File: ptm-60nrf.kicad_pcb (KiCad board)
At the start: 2 copper layers, 285 x 94.6 mm, 160 parts, among them J1 USB_C_Receptacle_USB2.0, J2 BAT, J4 SWD, Q1 AO3407, U1 TP4054, U2 XC6220B331MR-G, U3 nRF52840_holyiot_18010, U4 SRV05-4, Y1 32.768Hz

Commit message: fixed schematic flaws and caps lock (thanks Martin!)
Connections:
- MX32 pad 1: COL0 -> Net-(D33-Pad2)
- MX32 pad 2: Net-(D33-Pad2) -> COL0
- MX61 pad 1: Net-(MX61-Pad1) -> COL12
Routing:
- net COL0: track 282.5 -> 291.7 mm
- net Net-(D33-Pad2): track 15.7 -> 17.0 mm

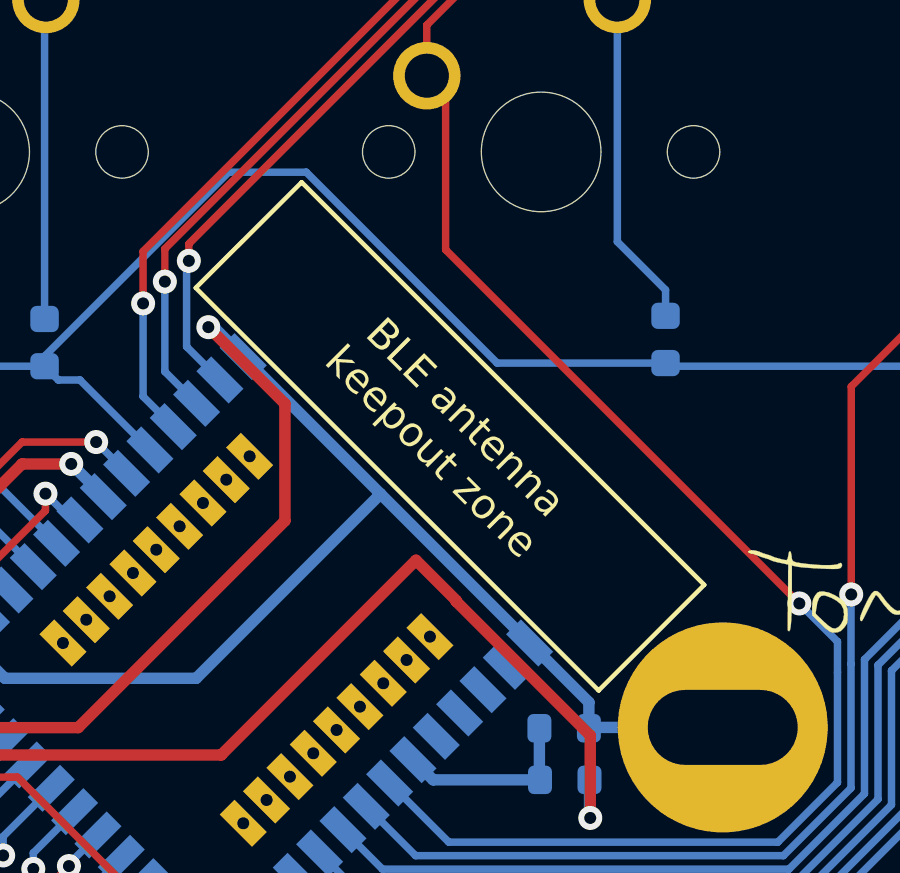
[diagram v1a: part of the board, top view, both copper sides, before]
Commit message: added hole for antenna
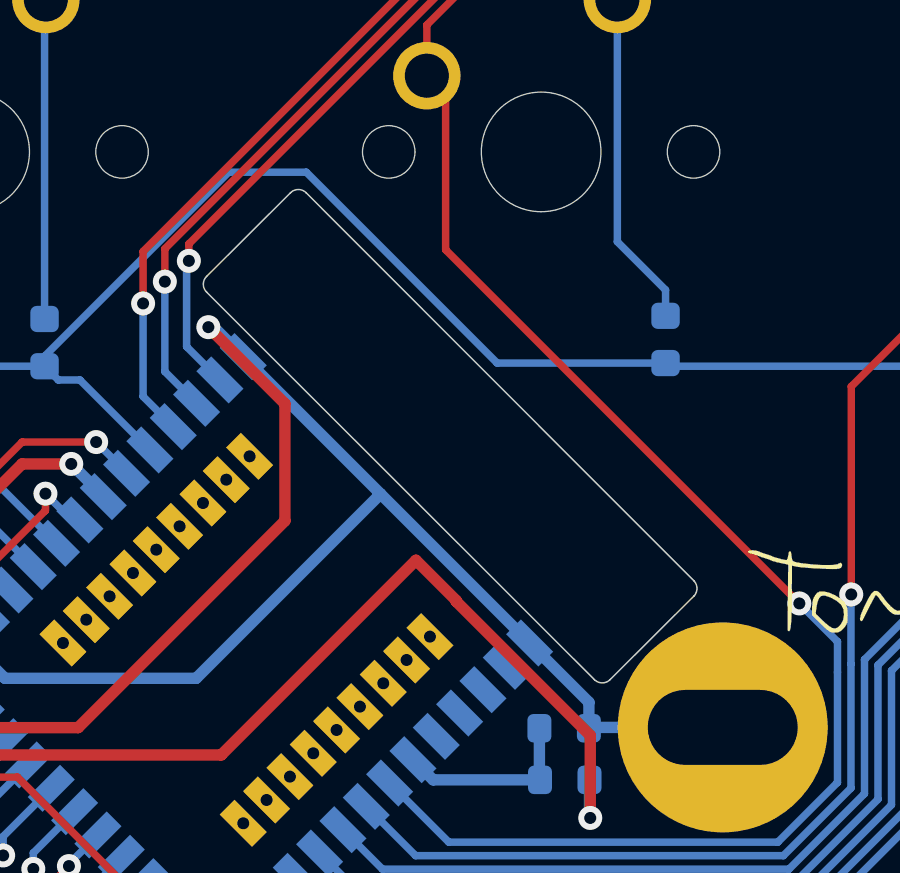
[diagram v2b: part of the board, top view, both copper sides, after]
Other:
- outline, holes or cut-outs redrawn
- board text removed: "BLE antenna keepout zone"
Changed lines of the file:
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@@
   (general
     (thickness 1.6)
-    (drawings 40)
+    (drawings 38)
     (tracks 951)
     (zones 0)
@@
     )
   )
+  (gr_line (start 209.599999 99.259999) (end 206.809999 102.039999) (layer Edge.Cuts) (width 0.05))
+  (gr_line (start 196.679999 85.810001) (end 209.599999 98.740001) (layer Edge.Cuts) (width 0.05))
+  (gr_line (start 193.360001 88.600001) (end 196.160001 85.810001) (layer Edge.Cuts) (width 0.05))
+  (gr_line (start 206.290001 102.039999) (end 193.360001 89.119999) (layer Edge.Cuts) (width 0.05))
+  (gr_arc (start 206.55 101.78) (end 206.290001 102.039999) (angle -90) (layer Edge.Cuts) (width 0.05))
+  (gr_arc (start 209.34 99) (end 209.599999 99.259999) (angle -90) (layer Edge.Cuts) (width 0.05))
+  (gr_arc (start 196.42 86.07) (end 196.679999 85.810001) (angle -90) (layer Edge.Cuts) (width 0.05))
+  (gr_arc (start 193.62 88.86) (end 193.360001 88.600001) (angle -90) (layer Edge.Cuts) (width 0.05))
   (gr_text BTW (at 301.94 109.39 90) (layer B.Mask)
     (effects (font (size 0.35 0.35) (thickness 0.04)) (justify mirror))
@@
     (effects (font (size 0.25 0.25) (thickness 0.05) italic) (justify mirror))
   )
-  (gr_line (start 192.99 88.97) (end 206.44 102.39) (layer B.SilkS) (width 0.12))
-  (gr_line (start 196.53 85.44) (end 192.99 88.97) (layer B.SilkS) (width 0.12))
-  (gr_line (start 209.96 98.88) (end 196.53 85.44) (layer B.SilkS) (width 0.12))
-  (gr_line (start 206.44 102.39) (end 209.96 98.88) (layer B.SilkS) (width 0.12))
-  (gr_text "BLE antenna\nkeepout zone" (at 201.44 93.87 -45) (layer B.SilkS)
-    (effects (font (size 1 1) (thickness 0.15)) (justify mirror))
-  )
-  (gr_line (start 209.95 98.88) (end 196.53 85.46) (layer F.SilkS) (width 0.15))
-  (gr_line (start 206.43 102.4) (end 209.95 98.88) (layer F.SilkS) (width 0.15))
-  (gr_line (start 193 88.98) (end 206.43 102.4) (layer F.SilkS) (width 0.15))
-  (gr_line (start 196.53 85.46) (end 193 88.98) (layer F.SilkS) (width 0.15))
-  (gr_text "BLE antenna\nkeepout zone" (at 201.43 93.87 315) (layer F.SilkS)
-    (effects (font (size 1 1) (thickness 0.15)))
-  )
   (gr_text Power (at 132.89 106.23) (layer B.Mask)

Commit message: minor fixes
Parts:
- removed G***: LOGO, tomlogo:tomlogoliten
- removed the HOLE at (45.2, 46.5)
- removed the HOLE at (210.6, 103.6)
- removed the HOLE at (277.9, 46.2)
- removed the HOLE at (147.3, 65.4)
- removed the HOLE at (303.4, 74.9)
- removed the HOLE at (19.7, 75.1)
- removed Y1: 32.768Hz, Crystal:Crystal_SMD_MicroCrystal_CM9V-T1A-2Pin_1.6x1.0mm
- added HOLE: VAL**, ptm-60nrf:PKRHSL, F.Cu at (303.4, 75.0)
- added HOLE: VAL**, ptm-60nrf:PKRH, F.Cu at (277.9, 46.2)
- added HOLE: VAL**, ptm-60nrf:PKRH, F.Cu at (147.4, 65.4)
- added HOLE: VAL**, ptm-60nrf:PKRH, F.Cu at (45.2, 46.5)
- added HOLE: VAL**, ptm-60nrf:PKRHSL, F.Cu at (19.6, 75.1)
- J4: footprint Connector_PinSocket_2.54mm:PinSocket_1x03_P2.54mm_Vertical -> Connector_PinSocket_2.54mm:PinSocket_1x04_P2.54mm_Vertical
- moved D31 16.2 mm to (265.0, 37.1), turned to 270 degrees
- moved D20 15.8 mm to (59.5, 37.1), turned to 270 degrees
- moved D21 15.8 mm to (78.5, 37.1), turned to 270 degrees
- moved D22 15.8 mm to (97.6, 37.1), turned to 270 degrees
- moved D23 15.8 mm to (116.6, 37.1), turned to 270 degrees
- moved D24 15.8 mm to (135.7, 37.1), turned to 270 degrees
- moved D25 15.8 mm to (154.7, 37.1), turned to 270 degrees
- moved D26 15.8 mm to (173.8, 37.1), turned to 270 degrees
- moved D27 15.8 mm to (192.8, 37.1), turned to 270 degrees
- moved D29 15.8 mm to (230.9, 37.1), turned to 270 degrees
- moved D30 15.8 mm to (250.0, 37.1), turned to 270 degrees
- moved D28 15.8 mm to (211.9, 37.1), turned to 270 degrees
- moved D59 15.1 mm to (207.1, 75.7), turned to 270 degrees
- moved D32 14.4 mm to (280.9, 38.5), turned to 0 degrees
- moved D19 14.1 mm to (32.5, 39.1), turned to 270 degrees
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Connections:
- J4 pad 1: Net-(J4-Pad1) -> GND
- J4 pad 2: /SWDCLK -> Net-(J4-Pad2)
- J4 pad 3: GND -> /SWDCLK
- MX33 pad 1: Net-(MX33-Pad1) -> COL1
- U3 pad 26: COL7 -> Net-(U3-Pad26)
- U3 pad 28: COL8 -> COL7
- U3 pad 29: Net-(U3-Pad29) -> COL8
- U3 pad 32: Net-(J4-Pad1) -> Net-(J4-Pad2)
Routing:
- net ROW1: track 291.0 -> 318.8 mm
- net VDD: track 70.1 -> 90.9 mm, vias 2 -> 3
- net Net-(J4-Pad2): track 0.00 -> 20.0 mm, vias 0 -> 1
- net Net-(J4-Pad1): track 16.6 -> 0.00 mm, vias 1 -> 0
- net ROW3: track 274.6 -> 288.1 mm
- net COL13: track 196.4 -> 208.4 mm
- net GND: track 372.0 -> 383.3 mm, vias 19 -> 21
- net COL9: track 121.9 -> 132.8 mm
- net COL1: track 236.9 -> 245.3 mm
- net Net-(D59-Pad2): track 11.3 -> 2.93 mm
- net Net-(D28-Pad2): track 10.8 -> 3.43 mm
- net Net-(D30-Pad2): track 10.8 -> 3.43 mm
- net Net-(D29-Pad2): track 10.8 -> 3.43 mm
- net Net-(D27-Pad2): track 10.8 -> 3.43 mm
- net Net-(D26-Pad2): track 10.8 -> 3.43 mm
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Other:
- board text added: "VDD"

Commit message: restored lost artwork
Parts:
- added G***: LOGO, ptm-60nrf:tomlogoliten, F.Cu at (223.5, 104.1)

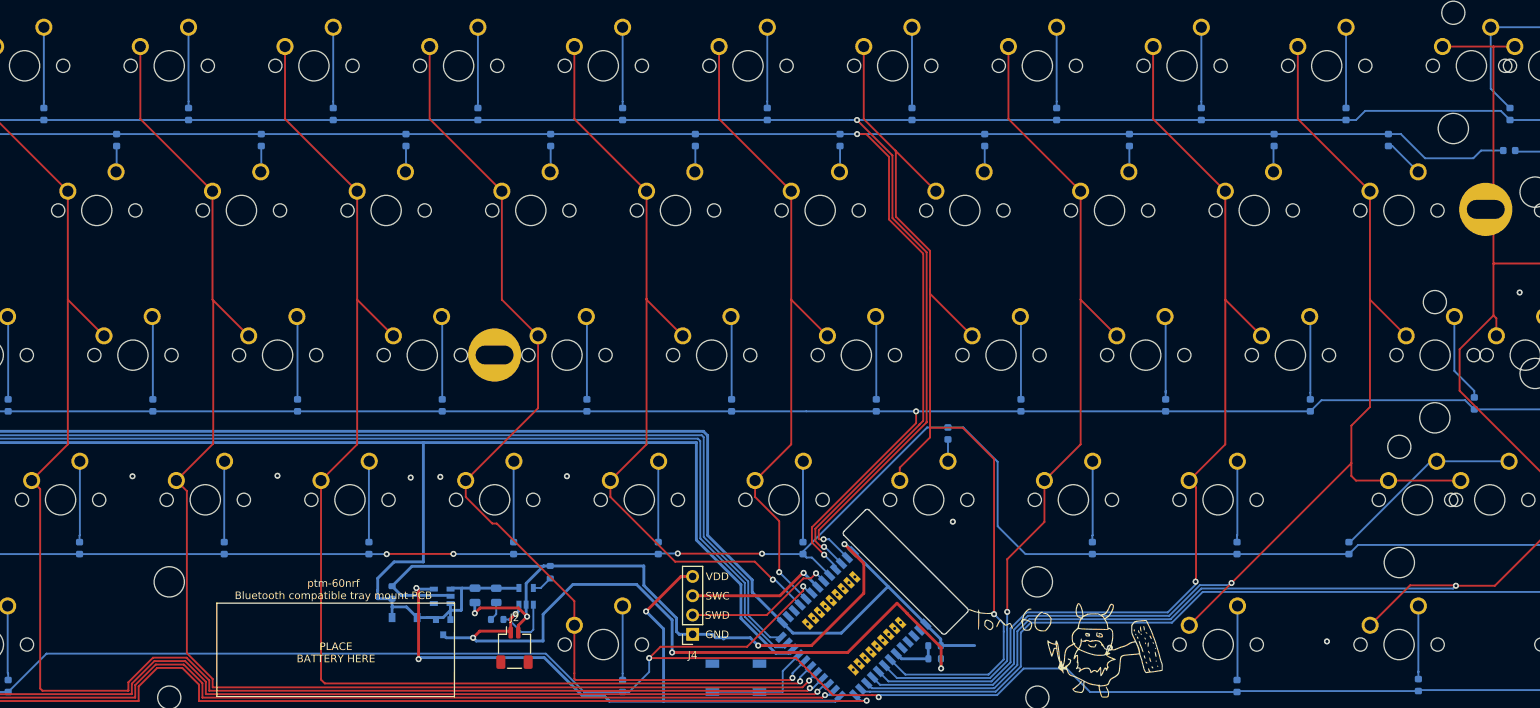
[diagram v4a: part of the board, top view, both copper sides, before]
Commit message: squashed bugs in schematic and rewired pwr/chrg
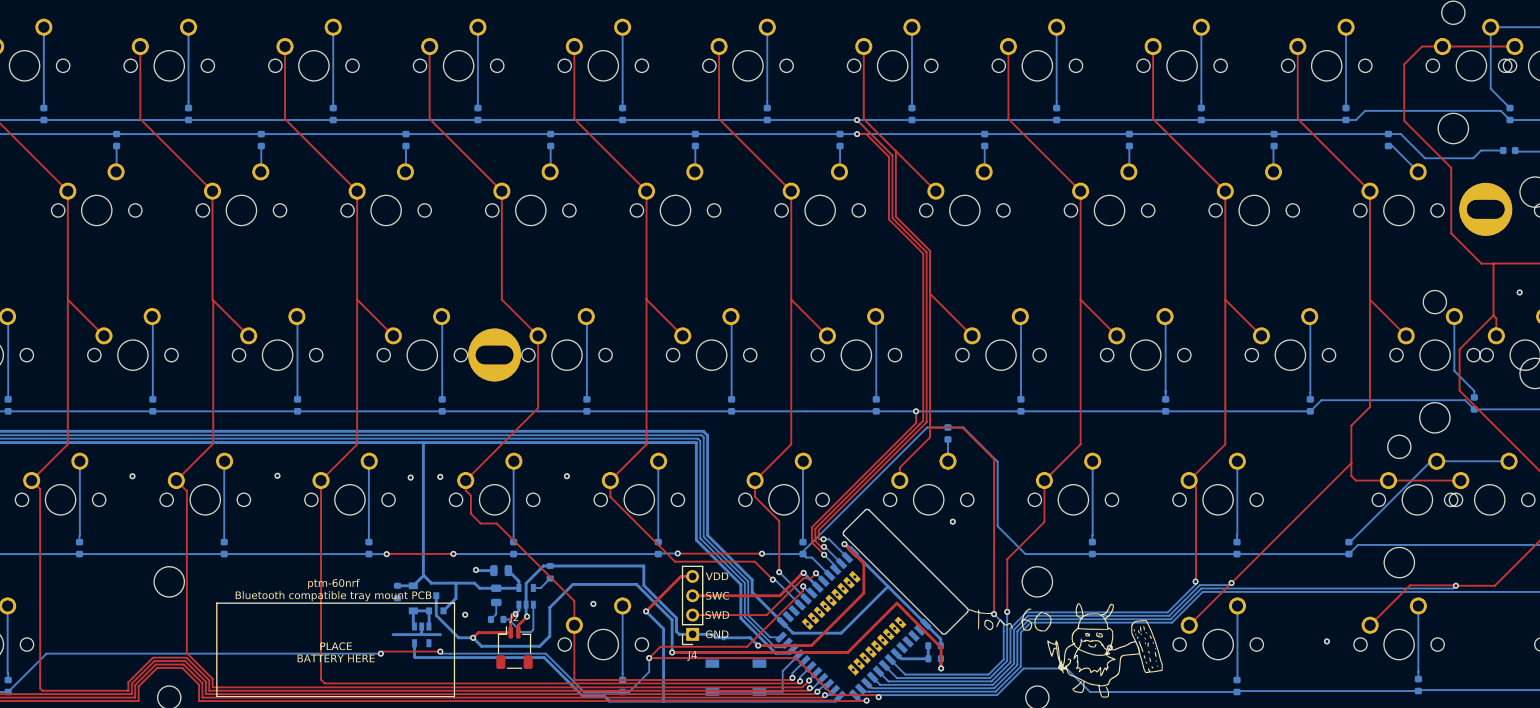
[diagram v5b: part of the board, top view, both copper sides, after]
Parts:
- moved U2 5.75 mm to (137.8, 102.2), turned to 270 degrees
- moved C1 4.74 mm to (148.2, 93.8), turned to 0 degrees
- moved Q1 3.28 mm to (139.7, 98.1), turned to 90 degrees
- moved D2 2.78 mm to (136.7, 97.4), turned to 90 degrees
- moved R3 0.72 mm to (134.6, 96.6), turned to 270 degrees
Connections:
- D2 pad 1: VBUS -> Net-(D2-Pad1)
- Q1 pad 2: VBUS -> Net-(D2-Pad1)
- U2 pad 1: VBUS -> Net-(D2-Pad1)
- U2 pad 3: VBUS -> Net-(D2-Pad1)
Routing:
- net GND: track 383.3 -> 350.4 mm, vias 21 -> 23
- net VBUS: track 285.7 -> 272.6 mm
- net VDD: track 90.9 -> 81.3 mm, vias 3 -> 1
- net COL13: track 208.4 -> 217.8 mm
- net Net-(D2-Pad1): track 0.00 -> 6.26 mm
- net VBAT: track 96.0 -> 101.1 mm
- net COL6: track 131.2 -> 132.1 mm
- net ROW4: track 295.5 -> 295.8 mm, vias 3 -> 5

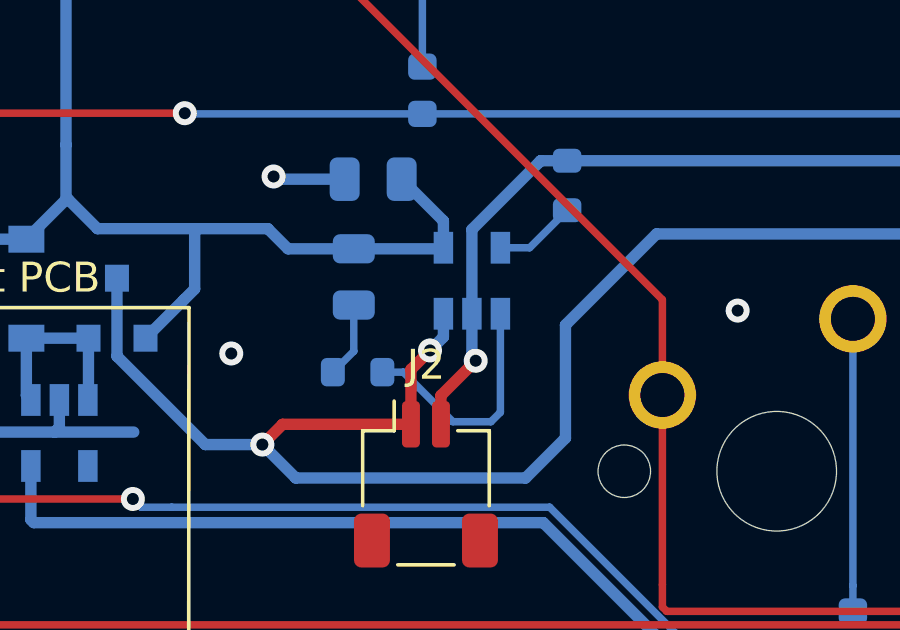
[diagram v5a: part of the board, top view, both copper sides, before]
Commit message: cosmetic changes and thicker traces in power block
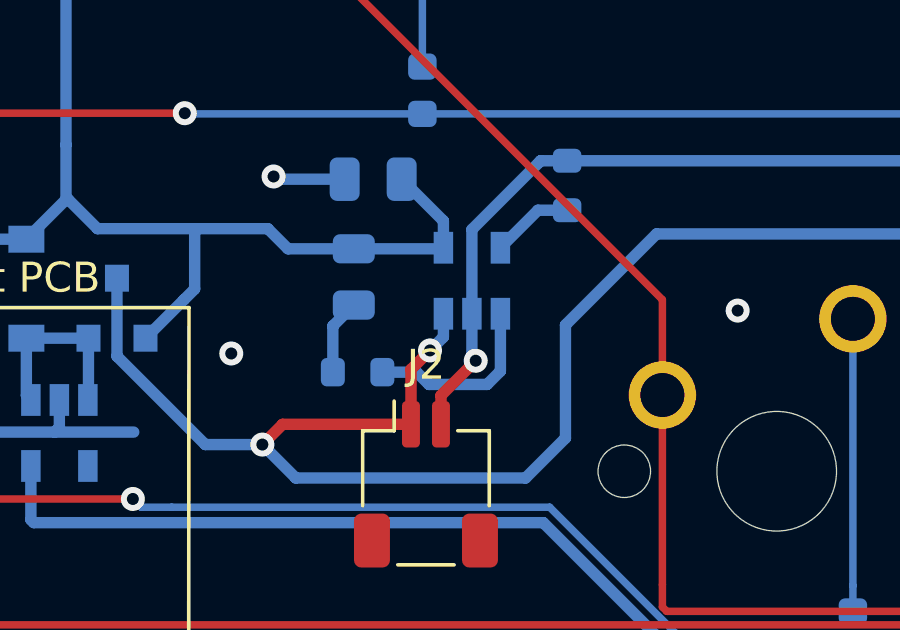
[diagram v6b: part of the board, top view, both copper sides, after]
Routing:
- net Net-(R1-Pad2): track 8.03 -> 6.20 mm
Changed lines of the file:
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@@
     (add_net COL8)
     (add_net COL9)
-    (add_net "Net-(D1-Pad1)")
     (add_net "Net-(D10-Pad2)")
     (add_net "Net-(D11-Pad2)")
@@
     (add_net "Net-(J1-PadB8)")
     (add_net "Net-(J4-Pad2)")
-    (add_net "Net-(R1-Pad2)")
-    (add_net "Net-(R2-Pad2)")
     (add_net "Net-(U2-Pad4)")
     (add_net "Net-(U3-Pad2)")
@@
     (add_net /VSENSE)
     (add_net GND)
+    (add_net "Net-(D1-Pad1)")
     (add_net "Net-(D2-Pad1)")
+    (add_net "Net-(R1-Pad2)")
+    (add_net "Net-(R2-Pad2)")
     (add_net VBAT)
     (add_net VBUS)
@@
   (segment (start 137.6 102.2) (end 140.24 102.2) (width 0.38) (layer B.Cu) (net 2))
   (via (at 160.37 98.15) (size 0.8) (drill 0.4) (layers F.Cu B.Cu) (net 2))
-  (segment (start 147.574 99.505) (end 146.876 100.203) (width 0.25) (layer B.Cu) (net 3))
-  (segment (start 147.574 97.9655) (end 147.574 99.505) (width 0.25) (layer B.Cu) (net 3))
+  (segment (start 146.876 98.6635) (end 147.574 97.9655) (width 0.38) (layer B.Cu) (net 3))
+  (segment (start 146.876 100.203) (end 146.876 98.6635) (width 0.38) (layer B.Cu) (net 3))
   (segment (start 30.861 22.225) (end 30.861 32.005) (width 0.25) (layer B.Cu) (net 4))
   (segment (start 30.861 32.8675) (end 30.861 32.005) (width 0.25) (layer B.Cu) (net 4))
@@
   (segment (start 287.02 45.66) (end 287.02 47.89) (width 0.25) (layer F.Cu) (net 95))
   (segment (start 288.28 44.4) (end 287.02 45.66) (width 0.25) (layer F.Cu) (net 95))
-  (segment (start 148.526 100.203) (end 149.225 100.203) (width 0.25) (layer B.Cu) (net 96))
-  (segment (start 149.225 100.203) (end 150.876 101.854) (width 0.25) (layer B.Cu) (net 96))
-  (segment (start 150.876 101.854) (end 152.146 101.854) (width 0.25) (layer B.Cu) (net 96))
-  (segment (start 152.461 101.539) (end 152.461 98.255) (width 0.25) (layer B.Cu) (net 96))
-  (segment (start 152.146 101.854) (end 152.461 101.539) (width 0.25) (layer B.Cu) (net 96))
-  (segment (start 153.436 96.055) (end 154.686 94.805) (width 0.25) (layer B.Cu) (net 97))
-  (segment (start 152.461 96.055) (end 153.436 96.055) (width 0.25) (layer B.Cu) (net 97))
+  (segment (start 152.461 100.168202) (end 152.461 98.255) (width 0.38) (layer B.Cu) (net 96))
+  (segment (start 152.017201 100.612001) (end 152.461 100.168202) (width 0.38) (layer B.Cu) (net 96))
+  (segment (start 150.078799 100.612001) (end 152.017201 100.612001) (width 0.38) (layer B.Cu) (net 96))
+  (segment (start 149.669798 100.203) (end 150.078799 100.612001) (width 0.38) (layer B.Cu) (net 96))
+  (segment (start 148.526 100.203) (end 149.669798 100.203) (width 0.38) (layer B.Cu) (net 96))
+  (segment (start 153.711 94.805) (end 152.461 96.055) (width 0.38) (layer B.Cu) (net 97))
+  (segment (start 154.686 94.805) (end 153.711 94.805) (width 0.38) (layer B.Cu) (net 97))
   (segment (start 204.455 105.36) (end 204.475 105.38) (width 0.38) (layer B.Cu) (net 98))
   (segment (start 204.455 103.66) (end 204.455 105.36) (width 0.38) (layer B.Cu) (net 98))

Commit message: cosmetic changes and removal of gnd in usb bus
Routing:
- net GND: track 350.4 -> 128.5 mm
- net COL5: track 161.9 -> 185.6 mm
- net COL6: track 132.1 -> 130.8 mm
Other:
- board text added: "Battery charging"
- board text added: "Power switching and filtering"

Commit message: some cosmetic changes - might revert some
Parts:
- moved D62 29.1 mm to (284.1, 74.8), turned to 270 degrees
- moved D51 19.9 mm to (47.0, 74.9), turned to 270 degrees
- moved D64 19.7 mm to (286.1, 74.8), turned to 270 degrees
- moved D53 19.4 mm to (81.7, 74.9), turned to 270 degrees
- moved D55 19.3 mm to (120.0, 74.8), turned to 270 degrees
- moved D61 19.2 mm to (234.4, 74.8), turned to 270 degrees
- moved D57 19.2 mm to (158.2, 74.9), turned to 270 degrees
- moved D49 18.2 mm to (44.4, 74.9), turned to 270 degrees
- moved D52 17.0 mm to (79.7, 74.9), turned to 270 degrees
- moved D58 17.0 mm to (193.8, 74.8), turned to 270 degrees
- moved D54 17.0 mm to (117.5, 74.8), turned to 270 degrees
- moved D60 17.0 mm to (231.8, 74.8), turned to 270 degrees
- moved D56 16.9 mm to (155.6, 74.9), turned to 270 degrees
- moved D46 16.1 mm to (260.3, 72.0)
- moved D68 15.6 mm to (159.9, 94.0), turned to 270 degrees
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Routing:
- net COL1: track 245.3 -> 313.8 mm
- net COL5: track 185.6 -> 251.3 mm
- net COL11: track 134.2 -> 199.5 mm
- net COL7: track 104.0 -> 157.0 mm
- net COL3: track 206.5 -> 252.7 mm
- net COL2: track 222.8 -> 266.0 mm
- net COL6: track 130.8 -> 172.7 mm
- net COL9: track 132.8 -> 169.1 mm
- net GND: track 128.5 -> 94.7 mm, vias 23 -> 22
- net COL12: track 168.9 -> 197.2 mm
- net COL4: track 179.3 -> 207.1 mm
- net COL0: track 292.9 -> 320.1 mm
- net COL8: track 88.2 -> 114.2 mm
- net COL10: track 113.4 -> 136.2 mm
- net Net-(D71-Pad2): track 9.61 -> 24.0 mm
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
